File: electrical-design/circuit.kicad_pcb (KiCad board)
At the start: 4 copper layers, 90 x 70 mm, 55 parts, among them J1 AVR-ISP-6, Q1 2N3906, Q2 2N3906, Q3 2N3906, Q4 2N3906, SW1 Reset Button, SW2 DS02C-254-1L-04BE, SW3 Reset Button, U1 ATmega8A-P, U2 LTC-4627JR, U3 NE555P, Y1 16MHz

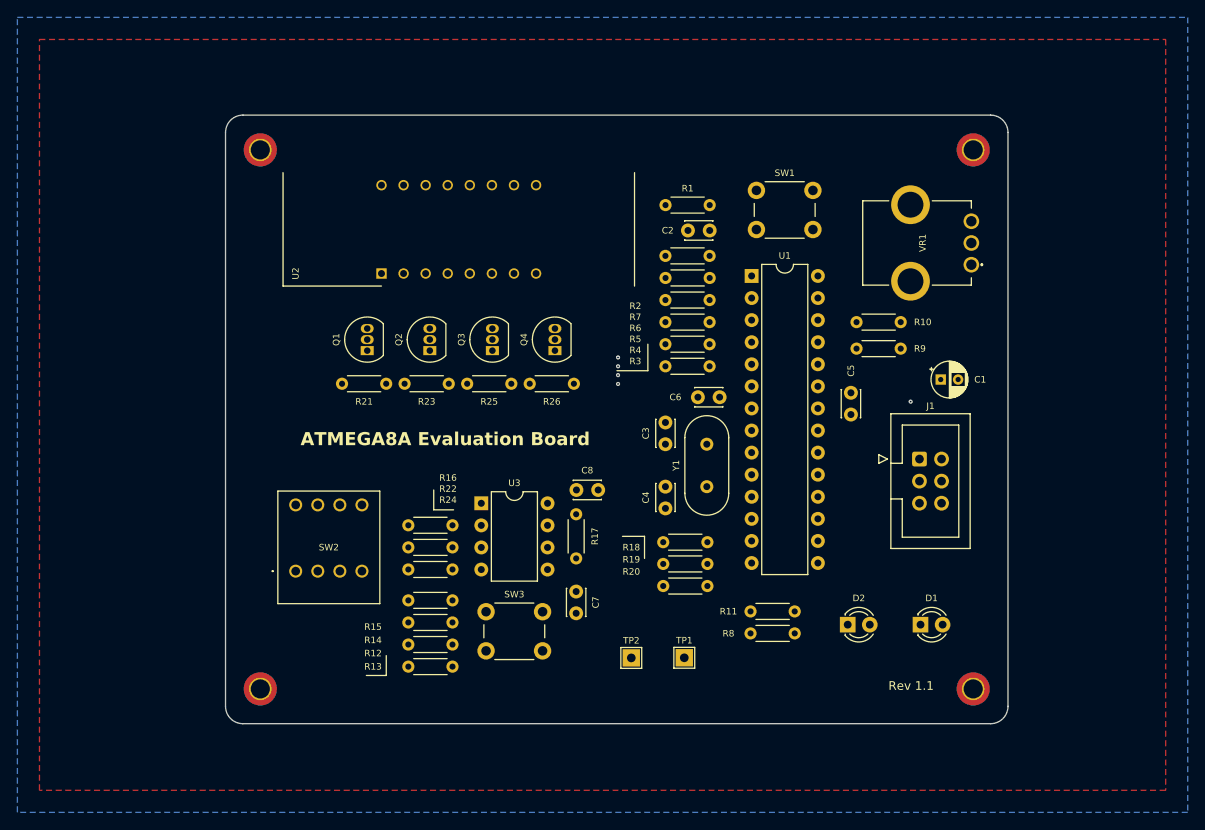
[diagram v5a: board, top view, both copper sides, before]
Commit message: Updated THT Resistor Footprint
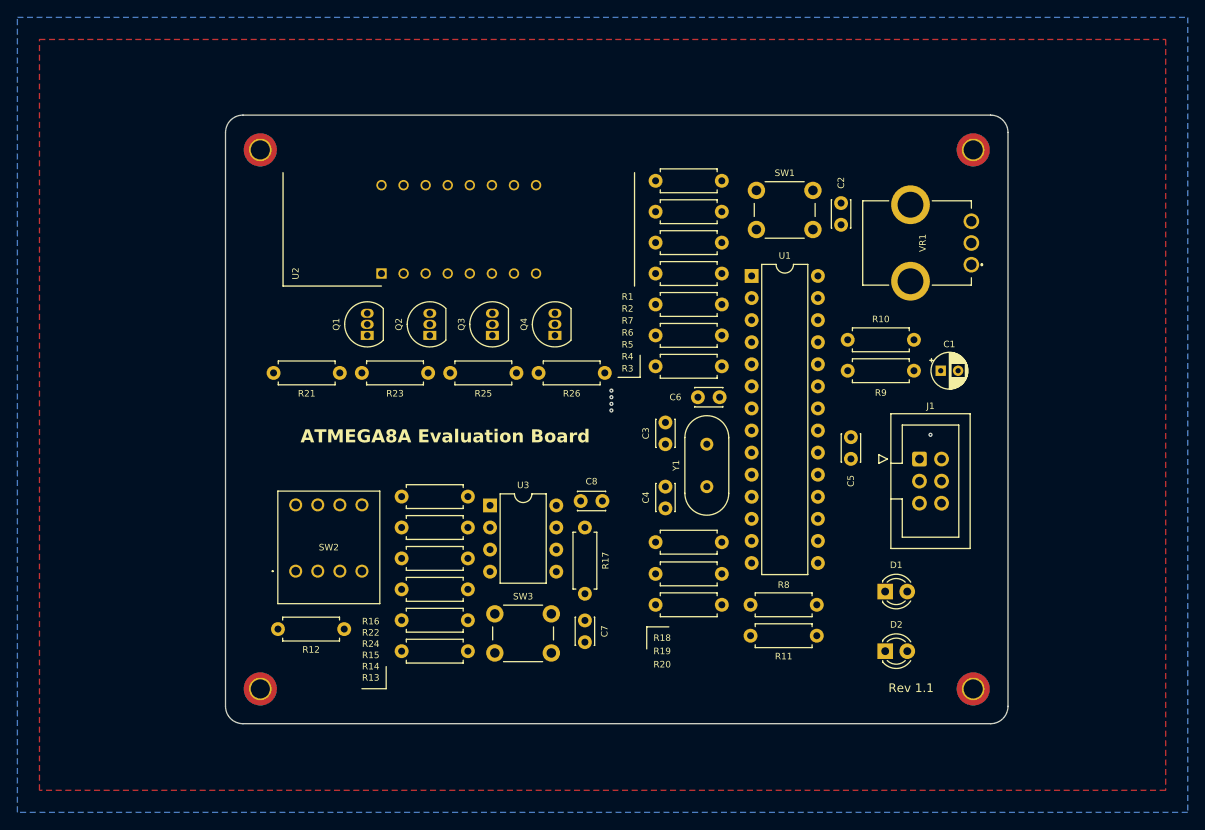
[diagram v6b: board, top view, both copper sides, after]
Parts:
- removed TP1: TP Frequency, TestPoint:TestPoint_THTPad_2.0x2.0mm_Drill1.0mm
- removed TP2: TP Ground, TestPoint:TestPoint_THTPad_2.0x2.0mm_Drill1.0mm
- R1, R10, R11, R12, R13, R14, R15, R16, R17, R18, R19, R2, R20, R21, R22, R23, R24, R25, R26, R3, R4, R5, R6, R7, R8, R9: footprint Resistor_THT:R_Axial_DIN0204_L3.6mm_D1.6mm_P5.08mm_Horizontal -> Resistor_THT:R_Axial_DIN0207_L6.3mm_D2.5mm_P7.62mm_Horizontal
- moved C2 17.9 mm to (127.8, 34.1), turned to -90 degrees
- moved R12 13.2 mm to (70.6, 83.1)
- moved C5 7.60 mm to (128.9, 63.5), turned to 90 degrees
- moved R7 7.43 mm to (106.4, 38.6), turned to 0 degrees
- moved R6 6.92 mm to (106.4, 42.2), turned to 0 degrees
- moved R5 6.54 mm to (106.4, 45.7), turned to 0 degrees
- moved R4 6.30 mm to (106.4, 49.3), turned to 0 degrees
- moved R3 6.21 mm to (106.4, 52.8), turned to 0 degrees
- moved D1 5.57 mm to (132.8, 78.7)
- moved R21 5.48 mm to (70.1, 53.6)
- moved D2 5.28 mm to (132.8, 85.6)
- moved R2 5.20 mm to (106.4, 35.1)
- moved R8 4.16 mm to (125.0, 80.3)
- moved R11 3.78 mm to (125.0, 83.8)
- moved R26 3.77 mm to (100.6, 53.6)
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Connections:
- R3 pad 1: /B -> Net-(U2-CATHODE_BL2)
- R3 pad 2: Net-(U2-CATHODE_BL2) -> /B
- R4 pad 1: /G -> Net-(U2-CATHODE_G)
- R4 pad 2: Net-(U2-CATHODE_G) -> /G
- R5 pad 1: /A -> Net-(U2-CATHODE_AL1)
- R5 pad 2: Net-(U2-CATHODE_AL1) -> /A
- R6 pad 1: /C -> Net-(U2-CATHODE_CL3)
- R6 pad 2: Net-(U2-CATHODE_CL3) -> /C
- R7 pad 1: /F -> Net-(U2-CATHODE_F)
- R7 pad 2: Net-(U2-CATHODE_F) -> /F
- U1 pad 15: Net-(D2-A) -> Net-(D1-A)
- U1 pad 16: Net-(D1-A) -> Net-(D2-A)
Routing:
- net Net-(D2-A): track 10.5 -> 22.5 mm
- net Frequency: track 47.3 -> 35.4 mm
- net Net-(SW2-COM1): track 17.5 -> 7.51 mm
- net Net-(D1-A): track 19.1 -> 11.6 mm
- net Net-(D1-K): track 15.7 -> 8.50 mm
- net Net-(Q1-B): track 6.66 -> 12.9 mm
- net ~{DIGIT_0}: track 52.9 -> 57.9 mm
- net ~{RESET}: track 62.6 -> 66.0 mm
- net Net-(Q2-B): track 6.87 -> 9.92 mm
- net Net-(SW2-NO1): track 35.7 -> 38.6 mm
- net Net-(U2-CATHODE_F): track 24.4 -> 21.6 mm
- net ~{DIGIT_1}: track 45.5 -> 48.2 mm
- net Net-(U2-CATHODE_CL3): track 30.5 -> 28.1 mm
- net /F: track 5.78 -> 7.79 mm
- net Net-(U2-CATHODE_AL1): track 34.1 -> 32.1 mm
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
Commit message: Completed Version 1.1
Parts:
- removed the C1 at (139.2, 53.3)
- J1: footprint Connector_IDC:IDC-Header_2x03_P2.54mm_Vertical -> Connector_PinHeader_2.54mm:PinHeader_2x03_P2.54mm_Vertical
- moved D2 6.87 mm to (137.2, 80.3)
- moved D1 3.17 mm to (130.0, 80.3)
- moved C4 0.29 mm to (129.0, 63.7)
- renumbered C2 to C1, C3 to C2, C4 to C3, C5 to C4, C6 to C5, C7 to C6, C8 to C7
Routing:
- net Net-(D2-K): track 8.61 -> 13.7 mm
- net Net-(D2-A): track 22.5 -> 18.8 mm
- net Net-(D1-K): track 8.50 -> 5.08 mm
- net Net-(D1-A): track 11.6 -> 10.7 mm
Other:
- board text added: "ATMEGA8A Tutorial Board A"
- board text added: "GND"
- board text added: "MISO"
- board text added: "MOSI"
- board text added: "SCK"
- board text added: "VCC"
- board text added: "~{RST}"
- board text removed: "ATMEGA8A Evaluation Board"

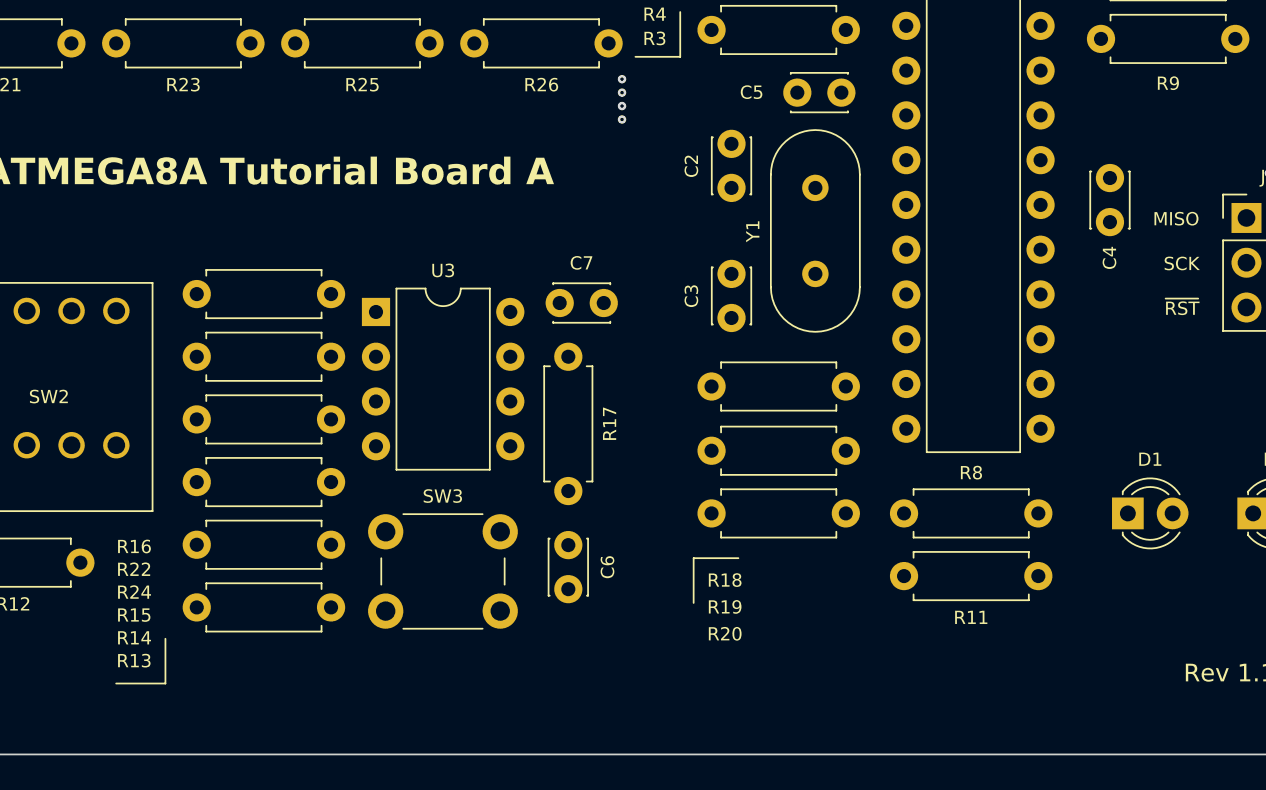
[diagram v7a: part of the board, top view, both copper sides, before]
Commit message: Added Input Protection on NE555 Timer
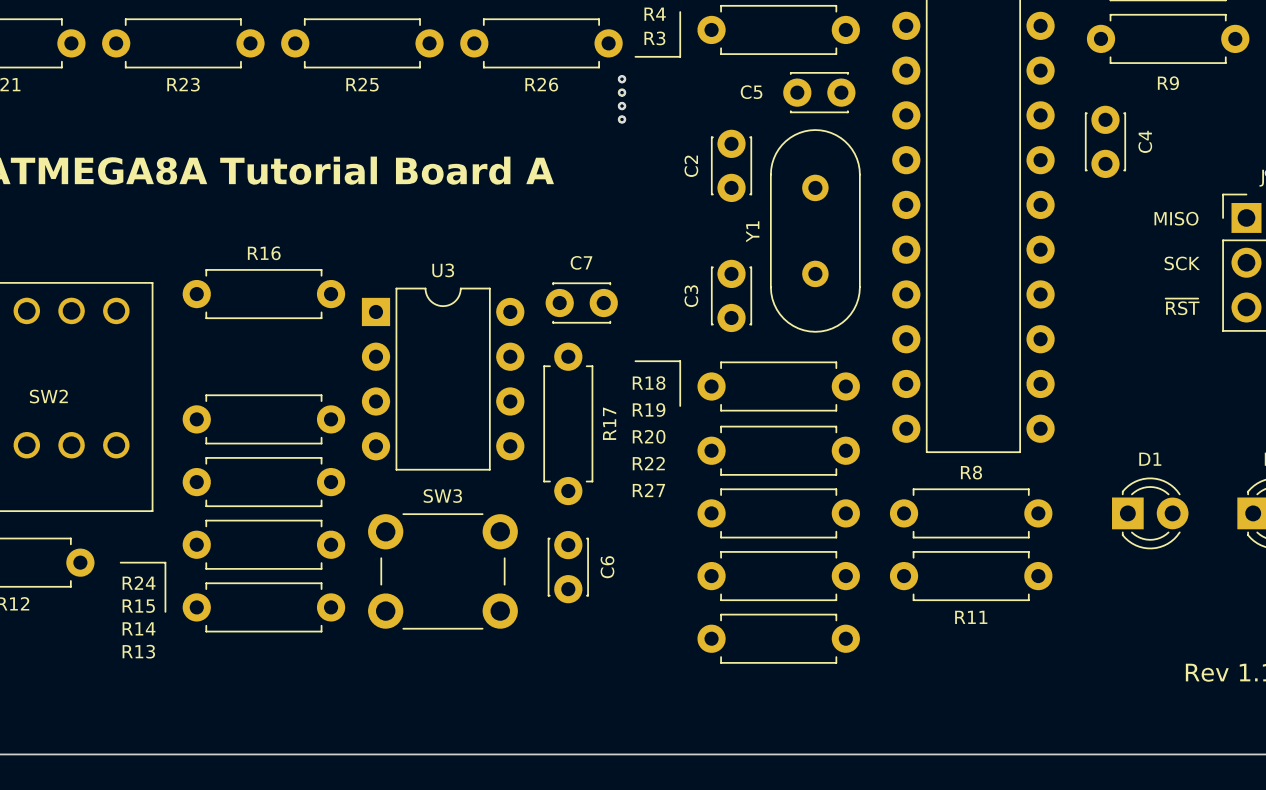
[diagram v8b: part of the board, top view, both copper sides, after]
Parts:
- added R27: 1K, Resistor_THT:R_Axial_DIN0207_L6.3mm_D2.5mm_P7.62mm_Horizontal, F.Cu at (114.0, 87.4)
- R22: value 10K -> 100K
- moved R22 38.9 mm to (114.0, 83.8), turned to 180 degrees
- moved C4 5.81 mm to (128.8, 57.9), turned to -90 degrees
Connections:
- R22 pad 1: VCC -> Frequency
- R22 pad 2: Frequency -> VCC
- U3 pad 3: Frequency -> Net-(U3-Q)
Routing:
- net Net-(U3-Q): track 0.00 -> 30.8 mm
- net Frequency: track 35.4 -> 18.0 mm
- net Net-(U1-AREF): track 4.36 -> 3.77 mm
